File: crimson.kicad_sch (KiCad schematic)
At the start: 0 parts

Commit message: [Schematics] initial Keyboard matrix
Signed-off-by: Lucy Mielke <user@domain.tld>
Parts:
- added D1, D10, D11, D12, D13, D14, D15, D16, D17, D18, D19, D2, D20, D21, D22, D23, D24, D25, D26, D27, D28, D29, D3, D30, D31, D32, D33, D34, D35, D36, D37, D38, D39, D4, D40, D41, D42, D43, D44, D45, D46, D47, D48, D49, D5, D50, D51, D52, D53, D54, D55, D56, D57, D58, D59, D6, D60, D61, D62, D63, D64, D65, D66, D67, D68, D69, D7, D70, D71, D72, D73, D74, D75, D76, D77, D78, D79, D8, D80, D81, D82, D83, D84, D85, D86, D87, D88, D89, D9, D90: 1N4148W, Diode_SMD:D_SOD-123, symbol Diode:1N4148W
- added SW1, SW10, SW11, SW12, SW13, SW14, SW15, SW16, SW17, SW18, SW19, SW2, SW20, SW21, SW22, SW23, SW24, SW25, SW26, SW27, SW28, SW29, SW3, SW30, SW31, SW32, SW33, SW34, SW35, SW36, SW37, SW38, SW39, SW4, SW40, SW41, SW42, SW43, SW44, SW45, SW46, SW47, SW48, SW49, SW5, SW50, SW51, SW52, SW53, SW54, SW55, SW56, SW57, SW58, SW59, SW6, SW60, SW61, SW62, SW63, SW64, SW65, SW66, SW67, SW68, SW69, SW7, SW70, SW71, SW72, SW73, SW74, SW75, SW76, SW77, SW78, SW79, SW8, SW80, SW81, SW82, SW83, SW84, SW85, SW86, SW87, SW88, SW89, SW9, SW90: SW_Push_Shielded, Cherry_ULP:Cherry_ULP_TH, symbol Switch:SW_Push_Shielded
- added U1: Nice!Nano v2, promicro:ProMicro, symbol nice_nano_v2:nice_nano_v2
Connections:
- new net: D59.2 (A), SW59.2
- new net: D37.2 (A), SW37.2
- new net: D89.2 (A), SW89.2
- new net: D20.2 (A), SW20.2
- new net: D6.2 (A), SW6.2
- new net: D76.2 (A), SW76.2
- new net: D50.2 (A), SW50.2
- new net: D19.2 (A), SW19.2
- new net: D51.2 (A), SW51.2
- new net: D88.2 (A), SW88.2
- new net: D72.2 (A), SW72.2
- new net: D5.2 (A), SW5.2
- new net: D87.2 (A), SW87.2
- new net: D75.2 (A), SW75.2
- new net: D85.2 (A), SW85.2
- new net: D15.2 (A), SW15.2
- new net: D56.2 (A), SW56.2
- new net: D78.2 (A), SW78.2
- new net: D21.2 (A), SW21.2
- new net: D65.2 (A), SW65.2
- new net: D42.2 (A), SW42.2
- new net: D26.2 (A), SW26.2
- new net: D49.2 (A), SW49.2
- new net: D4.2 (A), SW4.2
- new net: D61.2 (A), SW61.2
- new net: D29.2 (A), SW29.2
- new net: D12.2 (A), SW12.2
- new net: D57.2 (A), SW57.2
- new net: D8.2 (A), SW8.2
- new net: D41.2 (A), SW41.2
- new net: D2.2 (A), SW2.2
- new net: D23.2 (A), SW23.2
- new net: D36.2 (A), SW36.2
- new net: D77.2 (A), SW77.2
- new net: D45.2 (A), SW45.2
- new net: D83.2 (A), SW83.2
- new net: D17.2 (A), SW17.2
- new net: D67.2 (A), SW67.2
- new net: D18.2 (A), SW18.2
- new net: D81.2 (A), SW81.2
- new net: D25.2 (A), SW25.2
- new net: D62.2 (A), SW62.2
- new net: D10.2 (A), SW10.2
- new net: D64.2 (A), SW64.2
- new net: D71.2 (A), SW71.2
- new net: D32.2 (A), SW32.2
- new net: D48.2 (A), SW48.2
- new net: D44.2 (A), SW44.2
- new net: D82.2 (A), SW82.2
- new net: D35.2 (A), SW35.2
- new net: D16.2 (A), SW16.2
- new net: D14.2 (A), SW14.2
- new net: D55.2 (A), SW55.2
- new net: D69.2 (A), SW69.2
- new net: D66.2 (A), SW66.2
- new net: D52.2 (A), SW52.2
- new net: D90.2 (A), SW90.2
- new net: D58.2 (A), SW58.2
- new net: D24.2 (A), SW24.2
- new net: D34.2 (A), SW34.2
- new net: D43.2 (A), SW43.2
- new net: D53.2 (A), SW53.2
- new net: D63.2 (A), SW63.2
- new net: D46.2 (A), SW46.2
- new net: D13.2 (A), SW13.2
- new net: D84.2 (A), SW84.2
- new net: D28.2 (A), SW28.2
- new net: D31.2 (A), SW31.2
- new net: D7.2 (A), SW7.2
- new net: D1.2 (A), SW1.2
- new net: D40.2 (A), SW40.2
- new net: D27.2 (A), SW27.2
- new net: D68.2 (A), SW68.2
- new net: D38.2 (A), SW38.2
- new net: D3.2 (A), SW3.2
- new net: D11.2 (A), SW11.2
- new net: D30.2 (A), SW30.2
- new net: D33.2 (A), SW33.2
- new net: D47.2 (A), SW47.2
- new net: D9.2 (A), SW9.2
- new net: D86.2 (A), SW86.2
- new net: D73.2 (A), SW73.2
- new net: D70.2 (A), SW70.2
- new net: D22.2 (A), SW22.2
- new net: D54.2 (A), SW54.2
- new net: D60.2 (A), SW60.2
- new net: D74.2 (A), SW74.2
- new net: D39.2 (A), SW39.2
- new net: D80.2 (A), SW80.2
- new net: D79.2 (A), SW79.2
- new net COL0: SW1.1, SW10.1, SW21.1, SW22.1, SW41.1, SW42.1, SW43.1, SW44.1, SW81.1
- new net COL1: SW11.1, SW2.1, SW23.1, SW24.1, SW45.1, SW46.1, SW47.1, SW48.1, SW82.1
- new net COL2: SW12.1, SW25.1, SW26.1, SW3.1, SW49.1, SW50.1, SW51.1, SW52.1, SW83.1
- new net COL3: SW13.1, SW27.1, SW28.1, SW4.1, SW53.1, SW54.1, SW55.1, SW56.1, SW84.1
- new net COL4: SW14.1, SW29.1, SW30.1, SW5.1, SW57.1, SW58.1, SW59.1, SW60.1, SW85.1
- new net COL5: SW15.1, SW31.1, SW32.1, SW6.1, SW61.1, SW62.1, SW63.1, SW64.1, SW86.1
- new net COL6: SW16.1, SW33.1, SW34.1, SW65.1, SW66.1, SW67.1, SW68.1, SW7.1, SW87.1
- new net COL7: SW17.1, SW35.1, SW36.1, SW69.1, SW70.1, SW71.1, SW72.1, SW8.1, SW88.1
- new net COL8: SW18.1, SW37.1, SW38.1, SW73.1, SW74.1, SW75.1, SW76.1, SW89.1, SW9.1
- new net COL9: SW19.1, SW20.1, SW39.1, SW40.1, SW77.1, SW78.1, SW79.1, SW80.1, SW90.1
- new net ROW0: D1.1 (K), D19.1 (K), D2.1 (K), D3.1 (K), D4.1 (K), D5.1 (K), D6.1 (K), D7.1 (K), D8.1 (K), D9.1 (K)
- new net ROW1: D10.1 (K), D11.1 (K), D12.1 (K), D13.1 (K), D14.1 (K), D15.1 (K), D16.1 (K), D17.1 (K), D18.1 (K), D20.1 (K)
- new net ROW2: D21.1 (K), D23.1 (K), D25.1 (K), D27.1 (K), D29.1 (K), D31.1 (K), D33.1 (K), D35.1 (K), D37.1 (K), D39.1 (K)
- new net ROW3: D22.1 (K), D24.1 (K), D26.1 (K), D28.1 (K), D30.1 (K), D32.1 (K), D34.1 (K), D36.1 (K), D38.1 (K), D40.1 (K)
- new net ROW4: D41.1 (K), D45.1 (K), D49.1 (K), D53.1 (K), D57.1 (K), D61.1 (K), D65.1 (K), D69.1 (K), D73.1 (K), D77.1 (K)
- new net ROW5: D42.1 (K), D46.1 (K), D50.1 (K), D54.1 (K), D58.1 (K), D62.1 (K), D66.1 (K), D70.1 (K), D74.1 (K), D78.1 (K)
- new net ROW6: D43.1 (K), D47.1 (K), D51.1 (K), D55.1 (K), D59.1 (K), D63.1 (K), D67.1 (K), D71.1 (K), D75.1 (K), D79.1 (K)
- new net ROW7: D44.1 (K), D48.1 (K), D52.1 (K), D56.1 (K), D60.1 (K), D64.1 (K), D68.1 (K), D72.1 (K), D76.1 (K), D80.1 (K)
- new net ROW8: D81.1 (K), D82.1 (K), D83.1 (K), D84.1 (K), D85.1 (K), D86.1 (K), D87.1 (K), D88.1 (K), D89.1 (K), D90.1 (K)

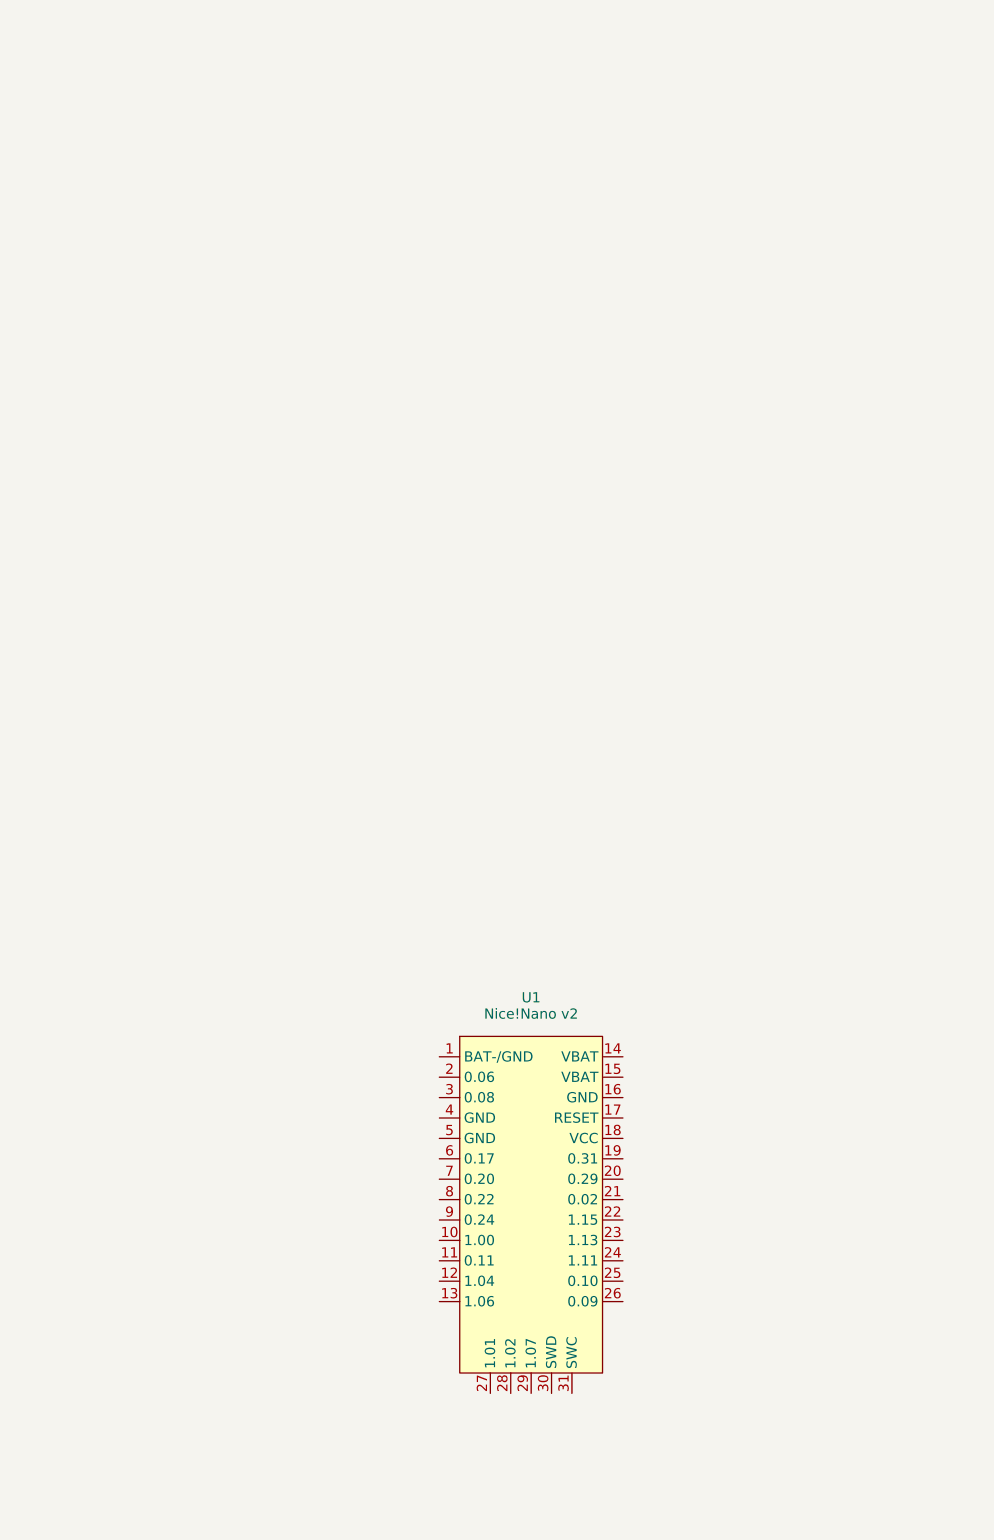
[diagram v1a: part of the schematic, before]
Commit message: [schematics] nice!nano v2 wired up and connected
The microcontroller "nice!nano v2" is now fully connected to the key
matrix.

Also, there's a tactile reset switch connected between RESET and GND,
as well as a JST battery connector, with an SPDT switch in between,
allowing the user to turn the keyboard off whenever it's necessary

Signed-off-by: Lucy Mielke <user@domain.tld>
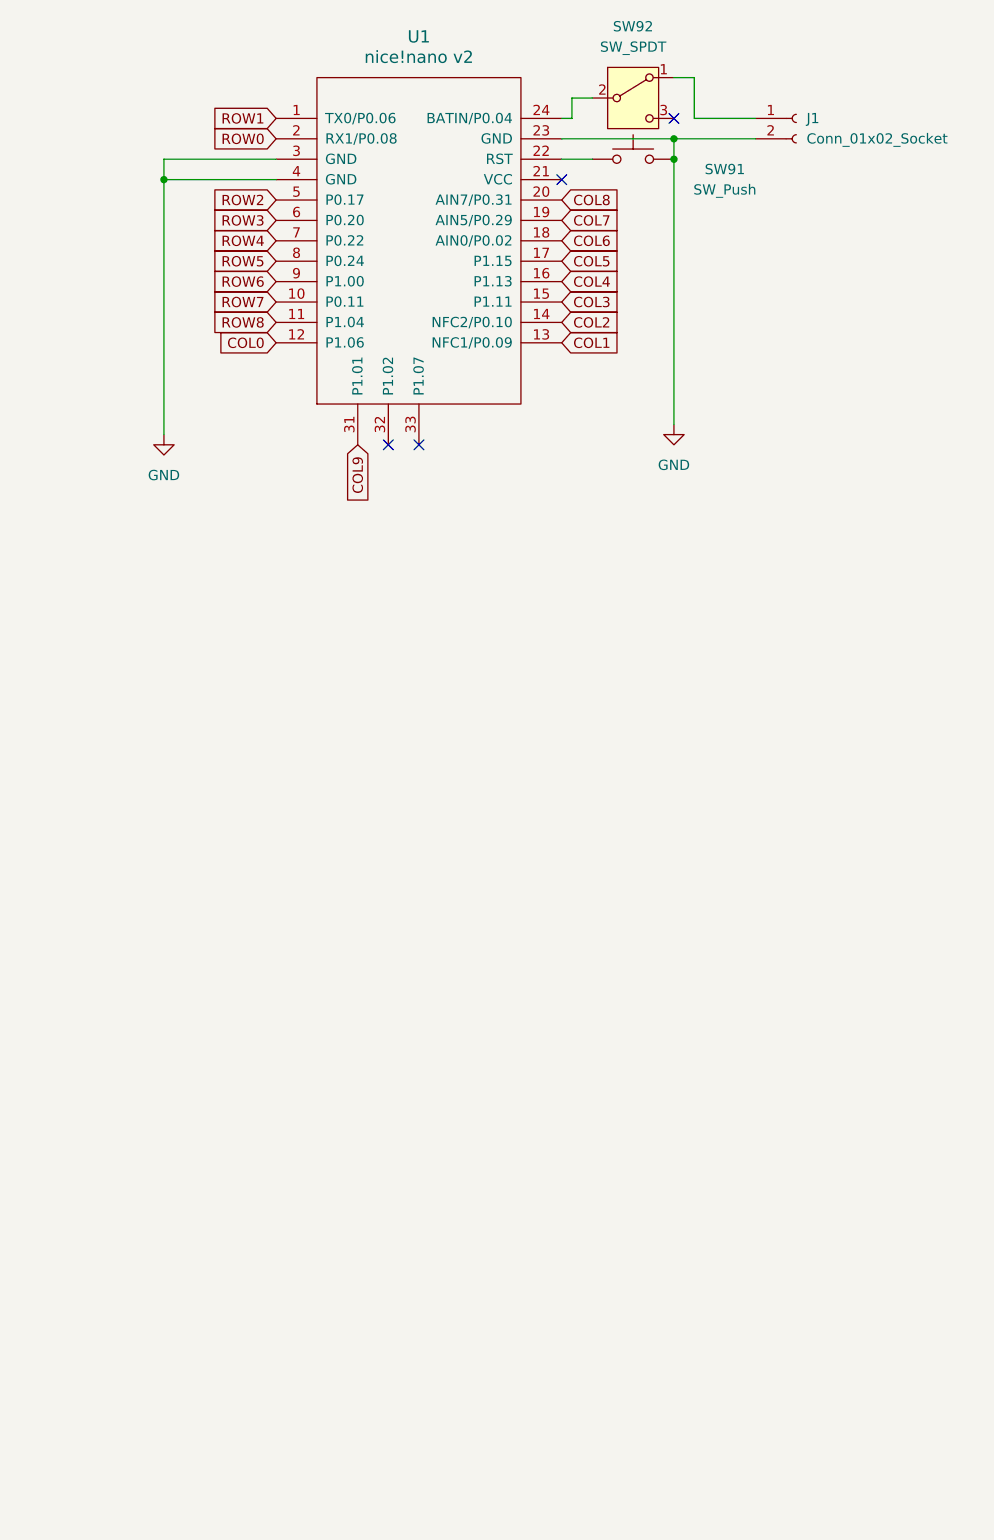
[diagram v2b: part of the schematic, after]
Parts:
- removed U1: Nice!Nano v2, promicro:ProMicro, symbol nice_nano_v2:nice_nano_v2
- added J1: Conn_01x02_Socket, Connector_JST:JST_PH_S2B-PH-K_1x02_P2.00mm_Horizontal, symbol Connector:Conn_01x02_Socket
- added SW91: SW_Push, Button_Switch_THT:SW_PUSH_6mm, symbol Switch:SW_Push
- added SW92: SW_SPDT, Button_Switch_SMD:SW_SPDT_PCM12, symbol Switch:SW_SPDT
- added U1: nice!nano v2, nice_nano:nice_nano, symbol nice!nano v2:nice_nano
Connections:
- net COL0: now also U1.12 (P1.06)
- net COL1: now also U1.13 (NFC1/P0.09)
- net COL2: now also U1.14 (NFC2/P0.10)
- net COL3: now also U1.15 (P1.11)
- net COL4: now also U1.16 (P1.13)
- net COL5: now also U1.17 (P1.15)
- net COL6: now also U1.18 (AIN0/P0.02)
- net COL7: now also U1.19 (AIN5/P0.29)
- net COL8: now also U1.20 (AIN7/P0.31)
- net COL9: now also U1.31 (P1.01)
- net ROW0: now also U1.2 (RX1/P0.08)
- net ROW1: now also U1.1 (TX0/P0.06)
- net ROW2: now also U1.5 (P0.17)
- net ROW3: now also U1.6 (P0.20)
- net ROW4: now also U1.7 (P0.22)
- net ROW5: now also U1.8 (P0.24)
- net ROW6: now also U1.9 (P1.00)
- net ROW7: now also U1.10 (P0.11)
- net ROW8: now also U1.11 (P1.04)
- new net: SW91.1, U1.22 (RST)
- new net: SW92.2 (B), U1.24 (BATIN/P0.04)
- new net: J1.1 (Pin_1), SW92.1 (A)
- new net GND: J1.2 (Pin_2), SW91.2, U1.23 (GND), U1.3 (GND), U1.4 (GND)
- no-connect marks 0 -> 4
